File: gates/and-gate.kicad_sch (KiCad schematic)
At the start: 7 parts, among them Q77 NPN, Q78 NPN, Q79 NPN

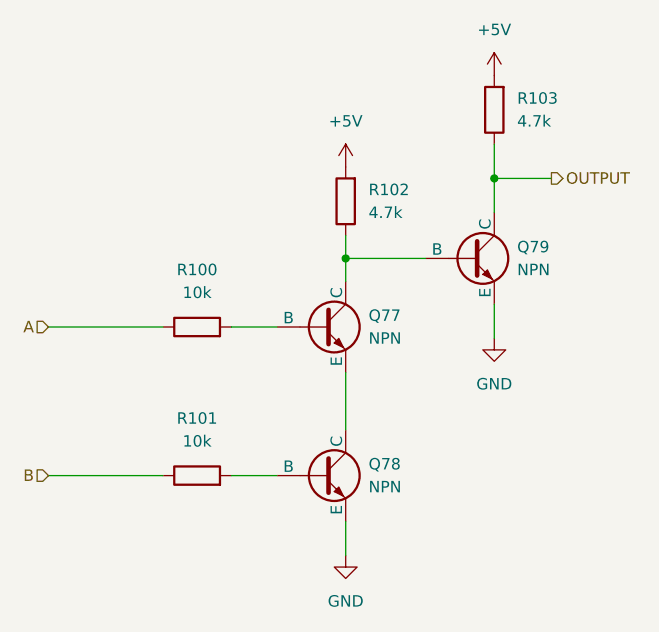
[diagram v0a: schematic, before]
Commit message: Implement logic for jump instruction
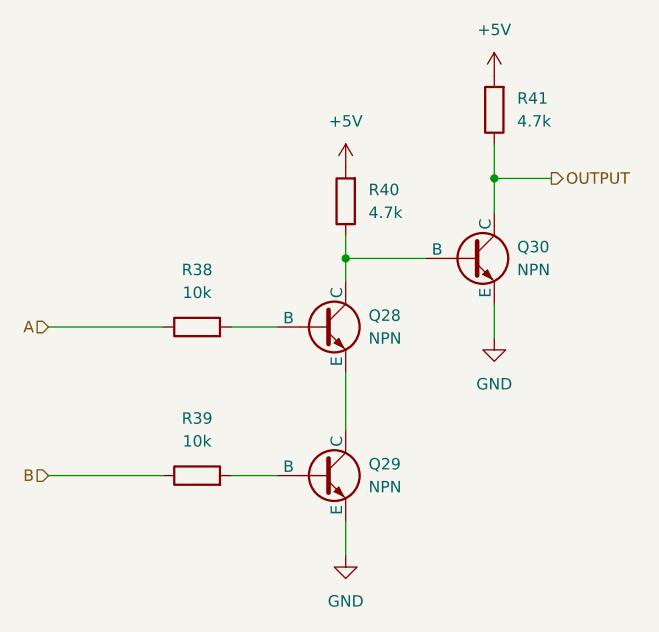
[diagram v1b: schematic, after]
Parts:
- renumbered Q77 to Q28, Q78 to Q29, Q79 to Q30, R100 to R38, R101 to R39, R102 to R40, R103 to R41
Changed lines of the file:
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@@
 		(dnp no)
 		(fields_autoplaced yes)
-		(property "Reference" "R103"
+		(property "Reference" "R41"
 			(at 132.08 46.9899 0)
 			(effects
@@
 		(instances
 			(project "control-unit"
-				(path "/1cf3a7ee-ec47-45b6-b515-1840d726ab8f/278c9957-db07-49b7-a219-9ad715efd000"
+				(path "/1cf3a7ee-ec47-45b6-b515-1840d726ab8f/33a494bb-4cba-4bf9-b8ca-9005632185f4"
+					(reference "R135")
+					(unit 1)
+				)
+				(path "/1cf3a7ee-ec47-45b6-b515-1840d726ab8f/65814c19-d7d1-4643-b724-38dde43cc39f"
 					(reference "R103")
-					(unit 1)
-				)
-				(path "/1cf3a7ee-ec47-45b6-b515-1840d726ab8f/293ab814-8224-438a-b8ef-17e439aa0d7e"
-					(reference "R107")
 					(unit 1)
 				)
@@
 		(dnp no)
 		(fields_autoplaced yes)
-		(property "Reference" "R101"
+		(property "Reference" "R39"
 			(at 96.52 82.55 90)
 			(effects
@@
 		(instances
 			(project "control-unit"
-				(path "/1cf3a7ee-ec47-45b6-b515-1840d726ab8f/278c9957-db07-49b7-a219-9ad715efd000"
+				(path "/1cf3a7ee-ec47-45b6-b515-1840d726ab8f/33a494bb-4cba-4bf9-b8ca-9005632185f4"
+					(reference "R133")
+					(unit 1)
+				)
+				(path "/1cf3a7ee-ec47-45b6-b515-1840d726ab8f/65814c19-d7d1-4643-b724-38dde43cc39f"
 					(reference "R101")
-					(unit 1)
-				)
-				(path "/1cf3a7ee-ec47-45b6-b515-1840d726ab8f/293ab814-8224-438a-b8ef-17e439aa0d7e"
-					(reference "R105")
 					(unit 1)
 				)
@@
 		(dnp no)
 		(fields_autoplaced yes)
-		(property "Reference" "#PWR091"
+		(property "Reference" "#PWR038"
 			(at 113.03 104.14 0)
 			(effects
@@
 		(instances
 			(project "control-unit"
-				(path "/1cf3a7ee-ec47-45b6-b515-1840d726ab8f/278c9957-db07-49b7-a219-9ad715efd000"
+				(path "/1cf3a7ee-ec47-45b6-b515-1840d726ab8f/33a494bb-4cba-4bf9-b8ca-9005632185f4"
+					(reference "#PWR0121")
+					(unit 1)
+				)
+				(path "/1cf3a7ee-ec47-45b6-b515-1840d726ab8f/65814c19-d7d1-4643-b724-38dde43cc39f"
 					(reference "#PWR091")
-					(unit 1)
-				)
-				(path "/1cf3a7ee-ec47-45b6-b515-1840d726ab8f/293ab814-8224-438a-b8ef-17e439aa0d7e"
-					(reference "#PWR095")
 					(unit 1)
 				)
@@
 		(dnp no)
 		(fields_autoplaced yes)
-		(property "Reference" "Q77"
+		(property "Reference" "Q28"
 			(at 115.57 71.1199 0)
 			(effects
@@
 		(instances
 			(project "control-unit"
-				(path "/1cf3a7ee-ec47-45b6-b515-1840d726ab8f/278c9957-db07-49b7-a219-9ad715efd000"
+				(path "/1cf3a7ee-ec47-45b6-b515-1840d726ab8f/33a494bb-4cba-4bf9-b8ca-9005632185f4"
+					(reference "Q99")
+					(unit 1)
+				)
+				(path "/1cf3a7ee-ec47-45b6-b515-1840d726ab8f/65814c19-d7d1-4643-b724-38dde43cc39f"
 					(reference "Q77")
-					(unit 1)
-				)
-				(path "/1cf3a7ee-ec47-45b6-b515-1840d726ab8f/293ab814-8224-438a-b8ef-17e439aa0d7e"
-					(reference "Q80")
 					(unit 1)
 				)
@@
 		(dnp no)
 		(fields_autoplaced yes)
-		(property "Reference" "#PWR093"
+		(property "Reference" "#PWR040"
 			(at 129.54 80.01 0)
 			(effects
@@
 		(instances
 			(project "control-unit"
-				(path "/1cf3a7ee-ec47-45b6-b515-1840d726ab8f/278c9957-db07-49b7-a219-9ad715efd000"
+				(path "/1cf3a7ee-ec47-45b6-b515-1840d726ab8f/33a494bb-4cba-4bf9-b8ca-9005632185f4"
+					(reference "#PWR0123")
+					(unit 1)
+				)
+				(path "/1cf3a7ee-ec47-45b6-b515-1840d726ab8f/65814c19-d7d1-4643-b724-38dde43cc39f"
 					(reference "#PWR093")
-					(unit 1)
-				)
-				(path "/1cf3a7ee-ec47-45b6-b515-1840d726ab8f/293ab814-8224-438a-b8ef-17e439aa0d7e"
-					(reference "#PWR097")
 					(unit 1)
 				)
@@
 		(dnp no)
 		(fields_autoplaced yes)
-		(property "Reference" "Q79"
+		(property "Reference" "Q30"
 			(at 132.08 63.4999 0)
 			(effects
@@
 		(instances
 			(project "control-unit"
-				(path "/1cf3a7ee-ec47-45b6-b515-1840d726ab8f/278c9957-db07-49b7-a219-9ad715efd000"
+				(path "/1cf3a7ee-ec47-45b6-b515-1840d726ab8f/33a494bb-4cba-4bf9-b8ca-9005632185f4"
+					(reference "Q101")
+					(unit 1)
+				)
+				(path "/1cf3a7ee-ec47-45b6-b515-1840d726ab8f/65814c19-d7d1-4643-b724-38dde43cc39f"
 					(reference "Q79")
-					(unit 1)
-				)
-				(path "/1cf3a7ee-ec47-45b6-b515-1840d726ab8f/293ab814-8224-438a-b8ef-17e439aa0d7e"
-					(reference "Q82")
 					(unit 1)
 				)
@@
 		(dnp no)
 		(fields_autoplaced yes)
-		(property "Reference" "R100"
+		(property "Reference" "R38"
 			(at 96.52 66.04 90)
 			(effects
@@
 		(instances
 			(project "control-unit"
-				(path "/1cf3a7ee-ec47-45b6-b515-1840d726ab8f/278c9957-db07-49b7-a219-9ad715efd000"
+				(path "/1cf3a7ee-ec47-45b6-b515-1840d726ab8f/33a494bb-4cba-4bf9-b8ca-9005632185f4"
+					(reference "R132")
+					(unit 1)
+				)
+				(path "/1cf3a7ee-ec47-45b6-b515-1840d726ab8f/65814c19-d7d1-4643-b724-38dde43cc39f"
 					(reference "R100")
-					(unit 1)
-				)
-				(path "/1cf3a7ee-ec47-45b6-b515-1840d726ab8f/293ab814-8224-438a-b8ef-17e439aa0d7e"
-					(reference "R104")
 					(unit 1)
 				)
@@
 		(dnp no)
 		(fields_autoplaced yes)
-		(property "Reference" "#PWR092"
+		(property "Reference" "#PWR039"
 			(at 129.54 48.26 0)
 			(effects
@@
 		(instances
 			(project "control-unit"
-				(path "/1cf3a7ee-ec47-45b6-b515-1840d726ab8f/278c9957-db07-49b7-a219-9ad715efd000"
+				(path "/1cf3a7ee-ec47-45b6-b515-1840d726ab8f/33a494bb-4cba-4bf9-b8ca-9005632185f4"
+					(reference "#PWR0122")
+					(unit 1)
+				)
+				(path "/1cf3a7ee-ec47-45b6-b515-1840d726ab8f/65814c19-d7d1-4643-b724-38dde43cc39f"
 					(reference "#PWR092")
-					(unit 1)
-				)
-				(path "/1cf3a7ee-ec47-45b6-b515-1840d726ab8f/293ab814-8224-438a-b8ef-17e439aa0d7e"
-					(reference "#PWR096")
 					(unit 1)
 				)
@@
 		(dnp no)
 		(fields_autoplaced yes)
-		(property "Reference" "#PWR090"
+		(property "Reference" "#PWR037"
 			(at 113.03 58.42 0)
 			(effects
@@
 		(instances
 			(project "control-unit"
-				(path "/1cf3a7ee-ec47-45b6-b515-1840d726ab8f/278c9957-db07-49b7-a219-9ad715efd000"
+				(path "/1cf3a7ee-ec47-45b6-b515-1840d726ab8f/33a494bb-4cba-4bf9-b8ca-9005632185f4"
+					(reference "#PWR0120")
+					(unit 1)
+				)
+				(path "/1cf3a7ee-ec47-45b6-b515-1840d726ab8f/65814c19-d7d1-4643-b724-38dde43cc39f"
 					(reference "#PWR090")
-					(unit 1)
-				)
-				(path "/1cf3a7ee-ec47-45b6-b515-1840d726ab8f/293ab814-8224-438a-b8ef-17e439aa0d7e"
-					(reference "#PWR094")
 					(unit 1)
 				)
@@
 		(dnp no)
 		(fields_autoplaced yes)
-		(property "Reference" "R102"
+		(property "Reference" "R40"
 			(at 115.57 57.1499 0)
 			(effects
@@
 		(instances
 			(project "control-unit"
-				(path "/1cf3a7ee-ec47-45b6-b515-1840d726ab8f/278c9957-db07-49b7-a219-9ad715efd000"
+				(path "/1cf3a7ee-ec47-45b6-b515-1840d726ab8f/33a494bb-4cba-4bf9-b8ca-9005632185f4"
+					(reference "R134")
+					(unit 1)
+				)
+				(path "/1cf3a7ee-ec47-45b6-b515-1840d726ab8f/65814c19-d7d1-4643-b724-38dde43cc39f"
 					(reference "R102")
-					(unit 1)
-				)
-				(path "/1cf3a7ee-ec47-45b6-b515-1840d726ab8f/293ab814-8224-438a-b8ef-17e439aa0d7e"
-					(reference "R106")
 					(unit 1)
 				)
@@
 		(dnp no)
 		(fields_autoplaced yes)
-		(property "Reference" "Q78"
+		(property "Reference" "Q29"
 			(at 115.57 87.6299 0)
 			(effects
@@
 		(instances
 			(project "control-unit"
-				(path "/1cf3a7ee-ec47-45b6-b515-1840d726ab8f/278c9957-db07-49b7-a219-9ad715efd000"
+				(path "/1cf3a7ee-ec47-45b6-b515-1840d726ab8f/33a494bb-4cba-4bf9-b8ca-9005632185f4"
+					(reference "Q100")
+					(unit 1)
+				)
+				(path "/1cf3a7ee-ec47-45b6-b515-1840d726ab8f/65814c19-d7d1-4643-b724-38dde43cc39f"
 					(reference "Q78")
 					(unit 1)
 				)
-				(path "/1cf3a7ee-ec47-45b6-b515-1840d726ab8f/293ab814-8224-438a-b8ef-17e439aa0d7e"
-					(reference "Q81")
-					(unit 1)
-				)

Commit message: Moved wires to more easily do operating point analysis
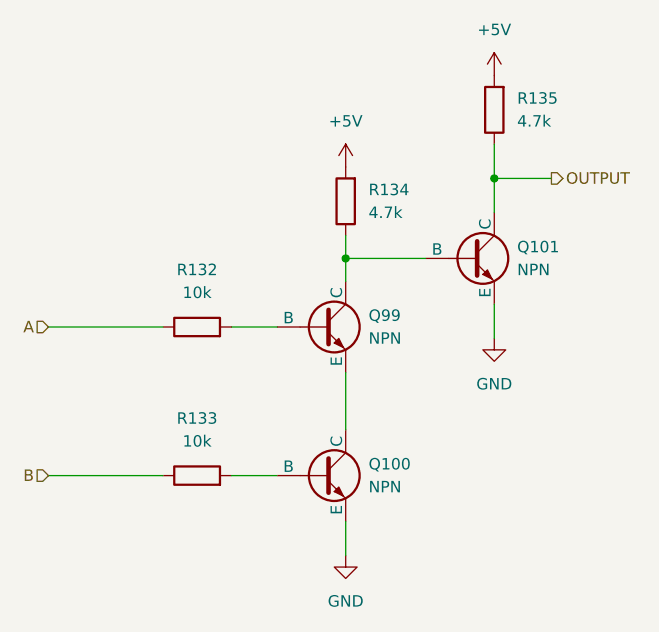
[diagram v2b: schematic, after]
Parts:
- renumbered Q29 to Q100, Q30 to Q101, Q28 to Q99, R38 to R132, R39 to R133, R40 to R134, R41 to R135
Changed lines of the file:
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@@
 		(dnp no)
 		(fields_autoplaced yes)
-		(property "Reference" "R41"
+		(property "Reference" "R135"
 			(at 132.08 46.9899 0)
 			(effects
@@
 		(dnp no)
 		(fields_autoplaced yes)
-		(property "Reference" "R39"
+		(property "Reference" "R133"
 			(at 96.52 82.55 90)
 			(effects
@@
 		(dnp no)
 		(fields_autoplaced yes)
-		(property "Reference" "#PWR038"
+		(property "Reference" "#PWR0121"
 			(at 113.03 104.14 0)
 			(effects
@@
 		(dnp no)
 		(fields_autoplaced yes)
-		(property "Reference" "Q28"
+		(property "Reference" "Q99"
 			(at 115.57 71.1199 0)
 			(effects
@@
 		(dnp no)
 		(fields_autoplaced yes)
-		(property "Reference" "#PWR040"
+		(property "Reference" "#PWR0123"
 			(at 129.54 80.01 0)
 			(effects
@@
 		(dnp no)
 		(fields_autoplaced yes)
-		(property "Reference" "Q30"
+		(property "Reference" "Q101"
 			(at 132.08 63.4999 0)
 			(effects
@@
 		(dnp no)
 		(fields_autoplaced yes)
-		(property "Reference" "R38"
+		(property "Reference" "R132"
 			(at 96.52 66.04 90)
 			(effects
@@
 		(dnp no)
 		(fields_autoplaced yes)
-		(property "Reference" "#PWR039"
+		(property "Reference" "#PWR0122"
 			(at 129.54 48.26 0)
 			(effects
@@
 		(dnp no)
 		(fields_autoplaced yes)
-		(property "Reference" "#PWR037"
+		(property "Reference" "#PWR0120"
 			(at 113.03 58.42 0)
 			(effects
@@
 		(dnp no)
 		(fields_autoplaced yes)
-		(property "Reference" "R40"
+		(property "Reference" "R134"
 			(at 115.57 57.1499 0)
 			(effects
@@
 		(dnp no)
 		(fields_autoplaced yes)
-		(property "Reference" "Q29"
+		(property "Reference" "Q100"
 			(at 115.57 87.6299 0)
 			(effects

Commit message: Use IC circuits in adder circuit
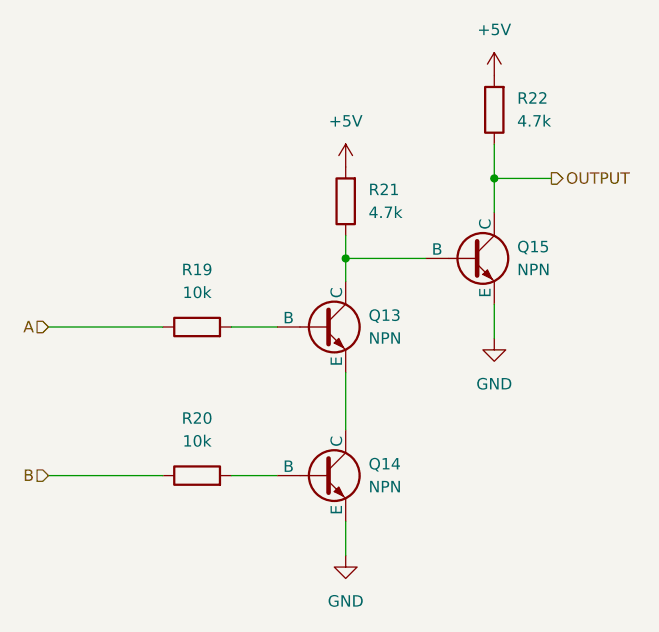
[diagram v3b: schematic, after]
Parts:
- renumbered Q99 to Q13, Q100 to Q14, Q101 to Q15, R132 to R19, R133 to R20, R134 to R21, R135 to R22
